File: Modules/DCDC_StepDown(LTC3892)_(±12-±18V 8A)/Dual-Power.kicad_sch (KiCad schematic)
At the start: 81 parts, among them J1 Conn_02x05_Top_Bottom, J2 Conn_02x05_Top_Bottom, J3 Conn_01x02, Q1 BSC028N06LS3, Q2 BSC028N06LS3, Q3 BSC028N06LS3, Q4 BSC028N06LS3, Q5 BSC028N06LS3, U1 LTC3892EUHPBF, U2 LT1797

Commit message: update Dual-Power components value
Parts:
- C4: value 2.2uF -> 4.7uF
- Cl1, Cl2: value OPT -> 100uF
- Cx1, Cx4, Cx5: value OPT -> 4.7uF
- Cx2, Cx3: value OPT -> 2.2uF
- Cx6, Cx7: value OPT -> 10uF
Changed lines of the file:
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@@
       (effects (font (size 1.27 1.27)) (justify left))
     )
-    (property "Value" "2.2uF" (id 1) (at 163.83 96.52 0)
+    (property "Value" "4.7uF" (id 1) (at 163.83 96.52 0)
       (effects (font (size 1.27 1.27)) (justify left))
     )
@@
       (effects (font (size 1.27 1.27)) (justify left))
     )
-    (property "Value" "OPT" (id 1) (at 330.2 52.07 0)
+    (property "Value" "4.7uF" (id 1) (at 330.2 52.07 0)
       (effects (font (size 1.27 1.27)) (justify left))
     )
@@
       (effects (font (size 1.27 1.27)) (justify left))
     )
-    (property "Value" "OPT" (id 1) (at 336.55 52.07 0)
+    (property "Value" "2.2uF" (id 1) (at 336.55 52.07 0)
       (effects (font (size 1.27 1.27)) (justify left))
     )
@@
       (effects (font (size 1.27 1.27)) (justify left))
     )
-    (property "Value" "OPT" (id 1) (at 342.9 52.07 0)
+    (property "Value" "2.2uF" (id 1) (at 342.9 52.07 0)
       (effects (font (size 1.27 1.27)) (justify left))
     )
@@
       (effects (font (size 1.27 1.27)) (justify left))
     )
-    (property "Value" "OPT" (id 1) (at 349.25 52.07 0)
+    (property "Value" "4.7uF" (id 1) (at 349.25 52.07 0)
       (effects (font (size 1.27 1.27)) (justify left))
     )
@@
       (effects (font (size 1.27 1.27)) (justify left))
     )
-    (property "Value" "OPT" (id 1) (at 355.6 52.07 0)
+    (property "Value" "4.7uF" (id 1) (at 355.6 52.07 0)
       (effects (font (size 1.27 1.27)) (justify left))
     )
@@
       (effects (font (size 1.27 1.27)) (justify left))
     )
-    (property "Value" "OPT" (id 1) (at 361.95 52.07 0)
+    (property "Value" "10uF" (id 1) (at 361.95 52.07 0)
       (effects (font (size 1.27 1.27)) (justify left))
     )
@@
       (effects (font (size 1.27 1.27)) (justify left))
     )
-    (property "Value" "OPT" (id 1) (at 368.3 52.07 0)
+    (property "Value" "10uF" (id 1) (at 368.3 52.07 0)
       (effects (font (size 1.27 1.27)) (justify left))
     )
@@
       (effects (font (size 1.27 1.27)) (justify right))
     )
-    (property "Value" "150uF" (id 1) (at 337.82 191.77 0)
+    (property "Value" "150uF" (id 1) (at 332.74 191.77 0)
       (effects (font (size 1.27 1.27)) (justify right))
     )
@@
       (effects (font (size 1.27 1.27)) (justify left))
     )
-    (property "Value" "OPT" (id 1) (at 372.11 52.07 0)
+    (property "Value" "100uF" (id 1) (at 372.11 52.07 0)
       (effects (font (size 1.27 1.27)) (justify left))
     )
@@
       (effects (font (size 1.27 1.27)) (justify left))
     )
-    (property "Value" "OPT" (id 1) (at 378.46 52.07 0)
+    (property "Value" "100uF" (id 1) (at 378.46 52.07 0)
       (effects (font (size 1.27 1.27)) (justify left))
     )
@@
     )
     (path "/00000000-0000-0000-0000-0000616375a2"
-      (reference "C4") (unit 1) (value "2.2uF") (footprint "Capacitor_SMD:C_1206_3216Metric")
+      (reference "C4") (unit 1) (value "4.7uF") (footprint "Capacitor_SMD:C_1206_3216Metric")
     )
     (path "/00000000-0000-0000-0000-0000616da52e"
@@
     )
     (path "/00000000-0000-0000-0000-0000617a732d"
-      (reference "Cl1") (unit 1) (value "OPT") (footprint "Capacitor_SMD:CP_Elec_10x10")
+      (reference "Cl1") (unit 1) (value "100uF") (footprint "Capacitor_SMD:CP_Elec_10x10")
     )
     (path "/00000000-0000-0000-0000-0000617a7327"
-      (reference "Cl2") (unit 1) (value "OPT") (footprint "Capacitor_SMD:CP_Elec_10x10")
+      (reference "Cl2") (unit 1) (value "100uF") (footprint "Capacitor_SMD:CP_Elec_10x10")
     )
     (path "/00000000-0000-0000-0000-0000617046a1"
-      (reference "Cx1") (unit 1) (value "OPT") (footprint "Capacitor_SMD:C_1206_3216Metric")
+      (reference "Cx1") (unit 1) (value "4.7uF") (footprint "Capacitor_SMD:C_1206_3216Metric")
     )
     (path "/00000000-0000-0000-0000-00006170469b"
-      (reference "Cx2") (unit 1) (value "OPT") (footprint "Capacitor_SMD:C_1206_3216Metric")
+      (reference "Cx2") (unit 1) (value "2.2uF") (footprint "Capacitor_SMD:C_1206_3216Metric")
     )
     (path "/00000000-0000-0000-0000-0000617dce4e"
-      (reference "Cx3") (unit 1) (value "OPT") (footprint "Capacitor_SMD:C_1206_3216Metric")
+      (reference "Cx3") (unit 1) (value "2.2uF") (footprint "Capacitor_SMD:C_1206_3216Metric")
     )
     (path "/00000000-0000-0000-0000-0000617dce48"
-      (reference "Cx4") (unit 1) (value "OPT") (footprint "Capacitor_SMD:C_1206_3216Metric")
+      (reference "Cx4") (unit 1) (value "4.7uF") (footprint "Capacitor_SMD:C_1206_3216Metric")
     )
     (path "/00000000-0000-0000-0000-0000618152fa"
-      (reference "Cx5") (unit 1) (value "OPT") (footprint "Capacitor_SMD:C_1206_3216Metric")
+      (reference "Cx5") (unit 1) (value "4.7uF") (footprint "Capacitor_SMD:C_1206_3216Metric")
     )
     (path "/00000000-0000-0000-0000-0000618152f4"
-      (reference "Cx6") (unit 1) (value "OPT") (footprint "Capacitor_SMD:C_1206_3216Metric")
+      (reference "Cx6") (unit 1) (value "10uF") (footprint "Capacitor_SMD:C_1206_3216Metric")
     )
     (path "/00000000-0000-0000-0000-000061871b5c"
-      (reference "Cx7") (unit 1) (value "OPT") (footprint "Capacitor_SMD:C_1206_3216Metric")
+      (reference "Cx7") (unit 1) (value "10uF") (footprint "Capacitor_SMD:C_1206_3216Metric")
     )
     (path "/00000000-0000-0000-0000-00006158ce04"

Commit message: fix description in Dual-Power.kicad_sch
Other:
- note added: "Q1\Q2\Q5 BSC028N OR BSC026N(Rec) Q3\Q4\ BSC100N OR BSC117N(Rec)"
- note removed: "Q1\Q2\Q5 BSC028N OR BSC026N Q3\Q4 BSC100N OR BSC117N"
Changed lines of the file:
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@@
+    (stroke (width 0) (type default) (color 0 0 0 0))
+  )
+  (polyline (pts (xy 264.16 199.39) (xy 303.53 199.39))
+    (stroke (width 0) (type default) (color 0 0 0 0))
+  )
+  (polyline (pts (xy 264.16 213.36) (xy 264.16 199.39))
     (stroke (width 0) (type default) (color 0 0 0 0))
   )
@@
     (stroke (width 0) (type default) (color 0 0 0 0))
   )
-  (polyline (pts (xy 265.43 196.85) (xy 300.99 196.85))
-    (stroke (width 0) (type default) (color 0 0 0 0))
-  )
-  (polyline (pts (xy 265.43 210.82) (xy 265.43 196.85))
-    (stroke (width 0) (type default) (color 0 0 0 0))
-  )
   (polyline (pts (xy 275.59 177.8) (xy 275.59 181.61))
     (stroke (width 0) (type default) (color 0 0 0 0))
@@
     (stroke (width 0) (type default) (color 0 0 0 0))
   )
-  (polyline (pts (xy 300.99 196.85) (xy 300.99 210.82))
+  (polyline (pts (xy 303.53 199.39) (xy 303.53 213.36))
     (stroke (width 0) (type default) (color 0 0 0 0))
   )
-  (polyline (pts (xy 300.99 210.82) (xy 265.43 210.82))
+  (polyline (pts (xy 303.53 213.36) (xy 264.16 213.36))
     (stroke (width 0) (type default) (color 0 0 0 0))
   )
@@
     (effects (font (size 1.27 1.27) (thickness 0.254) bold) (justify left bottom))
   )
-  (text "Group1: Q3 Q2 R14\nGroup2: Q4 Q5 R17 (Optional)" (at 266.7 201.93 0)
+  (text "Group1: Q3 Q2 R14\nGroup2: Q4 Q5 R17 (Optional)" (at 265.43 204.47 0)
     (effects (font (size 1.27 1.27)) (justify left bottom))
   )
-  (text "Q1\\Q2\\Q5 BSC028N OR BSC026N\nQ3\\Q4 BSC100N OR BSC117N"
-    (at 266.7 208.28 0)
+  (text "Q1\\Q2\\Q5 BSC028N OR BSC026N(Rec)\nQ3\\Q4\\   BSC100N OR BSC117N(Rec)"
+    (at 265.43 210.82 0)
     (effects (font (size 1.27 1.27)) (justify left bottom))
   )

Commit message: continue..
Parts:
- Q1, Q2, Q5: value BSC028N06LS3 -> BSC026N08NS5; symbol Transistor_FET:BSC028N06LS3 -> Transistor_FET:BSC026N08NS5
- Q3, Q4: value BSC028N06LS3 -> BSC117N08NS5; symbol Transistor_FET:BSC028N06LS3 -> Transistor_FET:BSC117N08NS5
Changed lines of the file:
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@@
     (pin "4")
   )
-  (symbol (lib_id "Transistor_FET:BSC028N06LS3") (at 168.91 179.07 180) (unit 1)
+  (symbol (lib_id "Transistor_FET:BSC026N08NS5") (at 168.91 179.07 180) (unit 1)
     (in_bom yes) (on_board yes)
     (property "Reference" "Q1" (id 0) (at 163.703 179.07 0)
       (effects (font (size 1.27 1.27)) (justify left))
     )
-    (property "Value" "BSC028N06LS3" (id 1) (at 163.7284 177.927 0)
+    (property "Value" "BSC026N08NS5" (id 1) (at 163.7284 177.927 0)
       (effects (font (size 1.27 1.27)) (justify left) hide)
     )
@@
       (effects (font (size 1.27 1.27) italic) (justify left) hide)
     )
-    (property "Datasheet" "http://www.infineon.com/dgdl/Infineon-BSC028N06LS3-DS-v02_02-en.pdf?fileId=db3a30431ddc9372011ebafa4c607f8c" (id 3) (at 168.91 179.07 90)
-      (effects (font (size 1.27 1.27)) (justify left) hide)
-    )
-    (pin "1")
-    (pin "2")
-    (pin "3")
-    (pin "4")
-    (pin "5")
-  )
-  (symbol (lib_id "Transistor_FET:BSC028N06LS3") (at 245.11 179.07 0) (unit 1)
+    (property "Datasheet" "http://www.infineon.com/dgdl/Infineon-BSC026N08NS5-DS-v02_01-EN.pdf?fileId=5546d4624ad04ef9014ae2eace7629e0" (id 3) (at 168.91 179.07 90)
+      (effects (font (size 1.27 1.27)) (justify left) hide)
+    )
+    (pin "1")
+    (pin "2")
+    (pin "3")
+    (pin "4")
+    (pin "5")
+  )
+  (symbol (lib_id "Transistor_FET:BSC117N08NS5") (at 245.11 179.07 0) (unit 1)
     (in_bom yes) (on_board yes)
     (property "Reference" "Q3" (id 0) (at 242.57 182.88 0)
       (effects (font (size 1.27 1.27)) (justify left))
     )
-    (property "Value" "BSC028N06LS3" (id 1) (at 250.2916 180.213 0)
+    (property "Value" "BSC117N08NS5" (id 1) (at 250.2916 180.213 0)
       (effects (font (size 1.27 1.27)) (justify left) hide)
     )
@@
       (effects (font (size 1.27 1.27) italic) (justify left) hide)
     )
-    (property "Datasheet" "http://www.infineon.com/dgdl/Infineon-BSC028N06LS3-DS-v02_02-en.pdf?fileId=db3a30431ddc9372011ebafa4c607f8c" (id 3) (at 245.11 179.07 90)
-      (effects (font (size 1.27 1.27)) (justify left) hide)
-    )
-    (pin "1")
-    (pin "2")
-    (pin "3")
-    (pin "4")
-    (pin "5")
-  )
-  (symbol (lib_id "Transistor_FET:BSC028N06LS3") (at 245.11 203.2 0) (unit 1)
+    (property "Datasheet" "http://www.infineon.com/dgdl/Infineon-BSC117N08NS5-DS-v02_00-EN.pdf?fileId=5546d4624ad04ef9014ae97632721c1b" (id 3) (at 245.11 179.07 90)
+      (effects (font (size 1.27 1.27)) (justify left) hide)
+    )
+    (pin "1")
+    (pin "2")
+    (pin "3")
+    (pin "4")
+    (pin "5")
+  )
+  (symbol (lib_id "Transistor_FET:BSC026N08NS5") (at 245.11 203.2 0) (unit 1)
     (in_bom yes) (on_board yes)
     (property "Reference" "Q2" (id 0) (at 242.57 199.39 0)
       (effects (font (size 1.27 1.27)) (justify left))
     )
-    (property "Value" "BSC028N06LS3" (id 1) (at 250.2916 204.343 0)
+    (property "Value" "BSC026N08NS5" (id 1) (at 250.2916 204.343 0)
       (effects (font (size 1.27 1.27)) (justify left) hide)
     )
@@
       (effects (font (size 1.27 1.27) italic) (justify left) hide)
     )
-    (property "Datasheet" "http://www.infineon.com/dgdl/Infineon-BSC028N06LS3-DS-v02_02-en.pdf?fileId=db3a30431ddc9372011ebafa4c607f8c" (id 3) (at 245.11 203.2 90)
-      (effects (font (size 1.27 1.27)) (justify left) hide)
-    )
-    (pin "1")
-    (pin "2")
-    (pin "3")
-    (pin "4")
-    (pin "5")
-  )
-  (symbol (lib_id "Transistor_FET:BSC028N06LS3") (at 257.81 179.07 0) (unit 1)
+    (property "Datasheet" "http://www.infineon.com/dgdl/Infineon-BSC026N08NS5-DS-v02_01-EN.pdf?fileId=5546d4624ad04ef9014ae2eace7629e0" (id 3) (at 245.11 203.2 90)
+      (effects (font (size 1.27 1.27)) (justify left) hide)
+    )
+    (pin "1")
+    (pin "2")
+    (pin "3")
+    (pin "4")
+    (pin "5")
+  )
+  (symbol (lib_id "Transistor_FET:BSC117N08NS5") (at 257.81 179.07 0) (unit 1)
     (in_bom yes) (on_board yes)
     (property "Reference" "Q4" (id 0) (at 255.27 182.88 0)
       (effects (font (size 1.27 1.27)) (justify left))
     )
-    (property "Value" "BSC028N06LS3" (id 1) (at 262.9916 180.213 0)
+    (property "Value" "BSC117N08NS5" (id 1) (at 262.9916 180.213 0)
       (effects (font (size 1.27 1.27)) (justify left) hide)
     )
@@
       (effects (font (size 1.27 1.27) italic) (justify left) hide)
     )
-    (property "Datasheet" "http://www.infineon.com/dgdl/Infineon-BSC028N06LS3-DS-v02_02-en.pdf?fileId=db3a30431ddc9372011ebafa4c607f8c" (id 3) (at 257.81 179.07 90)
-      (effects (font (size 1.27 1.27)) (justify left) hide)
-    )
-    (pin "1")
-    (pin "2")
-    (pin "3")
-    (pin "4")
-    (pin "5")
-  )
-  (symbol (lib_id "Transistor_FET:BSC028N06LS3") (at 257.81 203.2 0) (unit 1)
+    (property "Datasheet" "http://www.infineon.com/dgdl/Infineon-BSC117N08NS5-DS-v02_00-EN.pdf?fileId=5546d4624ad04ef9014ae97632721c1b" (id 3) (at 257.81 179.07 90)
+      (effects (font (size 1.27 1.27)) (justify left) hide)
+    )
+    (pin "1")
+    (pin "2")
+    (pin "3")
+    (pin "4")
+    (pin "5")
+  )
+  (symbol (lib_id "Transistor_FET:BSC026N08NS5") (at 257.81 203.2 0) (unit 1)
     (in_bom yes) (on_board yes)
     (property "Reference" "Q5" (id 0) (at 255.27 199.39 0)
       (effects (font (size 1.27 1.27)) (justify left))
     )
-    (property "Value" "BSC028N06LS3" (id 1) (at 262.9916 204.343 0)
+    (property "Value" "BSC026N08NS5" (id 1) (at 262.9916 204.343 0)
       (effects (font (size 1.27 1.27)) (justify left) hide)
     )
@@
       (effects (font (size 1.27 1.27) italic) (justify left) hide)
     )
-    (property "Datasheet" "http://www.infineon.com/dgdl/Infineon-BSC028N06LS3-DS-v02_02-en.pdf?fileId=db3a30431ddc9372011ebafa4c607f8c" (id 3) (at 257.81 203.2 90)
+    (property "Datasheet" "http://www.infineon.com/dgdl/Infineon-BSC026N08NS5-DS-v02_01-EN.pdf?fileId=5546d4624ad04ef9014ae2eace7629e0" (id 3) (at 257.81 203.2 90)
       (effects (font (size 1.27 1.27)) (justify left) hide)
     )
@@
     )
     (path "/00000000-0000-0000-0000-00006185bead"
-      (reference "Q1") (unit 1) (value "BSC028N06LS3") (footprint "Package_TO_SOT_SMD:TDSON-8-1")
+      (reference "Q1") (unit 1) (value "BSC026N08NS5") (footprint "Package_TO_SOT_SMD:TDSON-8-1")
     )
     (path "/00000000-0000-0000-0000-00006156edf6"
-      (reference "Q2") (unit 1) (value "BSC028N06LS3") (footprint "Package_TO_SOT_SMD:TDSON-8-1")
+      (reference "Q2") (unit 1) (value "BSC026N08NS5") (footprint "Package_TO_SOT_SMD:TDSON-8-1")
     )
     (path "/00000000-0000-0000-0000-00006167a267"
-      (reference "Q3") (unit 1) (value "BSC028N06LS3") (footprint "Package_TO_SOT_SMD:TDSON-8-1")
+      (reference "Q3") (unit 1) (value "BSC117N08NS5") (footprint "Package_TO_SOT_SMD:TDSON-8-1")
     )
     (path "/00000000-0000-0000-0000-00006160bac2"
-      (reference "Q4") (unit 1) (value "BSC028N06LS3") (footprint "Package_TO_SOT_SMD:TDSON-8-1")
+      (reference "Q4") (unit 1) (value "BSC117N08NS5") (footprint "Package_TO_SOT_SMD:TDSON-8-1")
     )
     (path "/00000000-0000-0000-0000-00006162e77f"
-      (reference "Q5") (unit 1) (value "BSC028N06LS3") (footprint "Package_TO_SOT_SMD:TDSON-8-1")
+      (reference "Q5") (unit 1) (value "BSC026N08NS5") (footprint "Package_TO_SOT_SMD:TDSON-8-1")
     )
     (path "/00000000-0000-0000-0000-0000615fa318"

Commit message: DCDC_StepDown(TLC3892) > fix capacity value
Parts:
- C4: value 4.7uF -> 2.2uF
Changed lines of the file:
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@@
       (effects (font (size 1.27 1.27)) (justify left))
     )
-    (property "Value" "4.7uF" (id 1) (at 163.83 96.52 0)
+    (property "Value" "2.2uF" (id 1) (at 163.83 96.52 0)
       (effects (font (size 1.27 1.27)) (justify left))
     )
@@
     )
     (path "/00000000-0000-0000-0000-0000616375a2"
-      (reference "C4") (unit 1) (value "4.7uF") (footprint "Capacitor_SMD:C_1206_3216Metric")
+      (reference "C4") (unit 1) (value "2.2uF") (footprint "Capacitor_SMD:C_1206_3216Metric")
     )
     (path "/00000000-0000-0000-0000-0000616da52e"

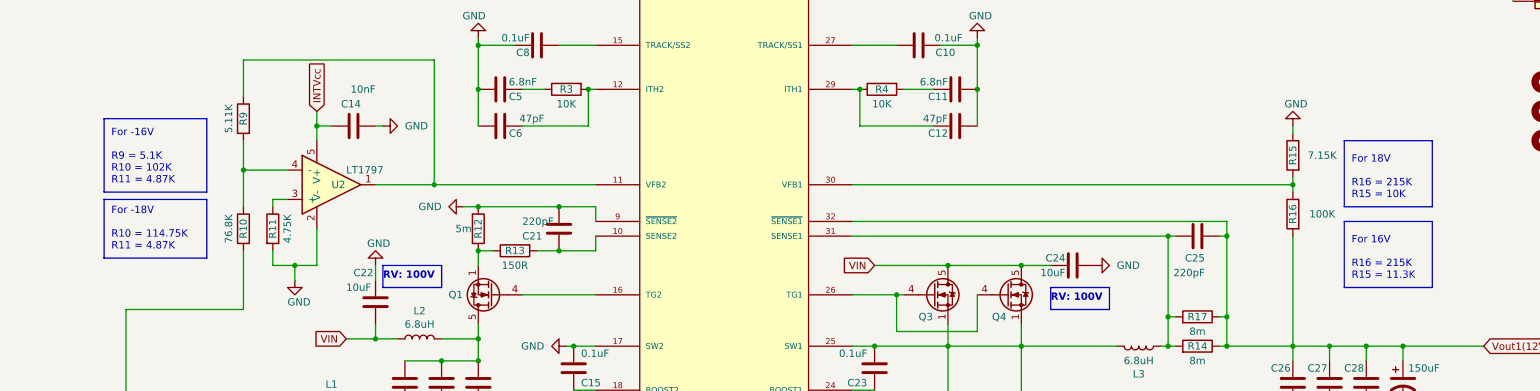
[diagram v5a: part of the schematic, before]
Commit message: Update description in Sch
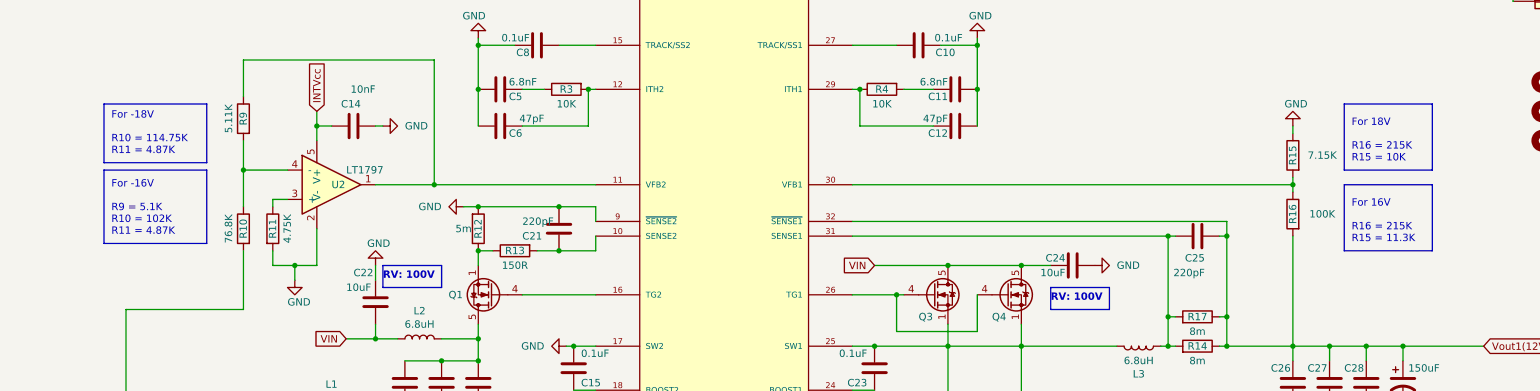
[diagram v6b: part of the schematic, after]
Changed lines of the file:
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@@
     (stroke (width 0) (type default) (color 0 0 0 0))
   )
-  (polyline (pts (xy 316.23 177.8) (xy 331.47 177.8))
+  (polyline (pts (xy 316.23 171.45) (xy 331.47 171.45))
     (stroke (width 0) (type default) (color 0 0 0 0))
   )
@@
     (stroke (width 0) (type default) (color 0 0 0 0))
   )
-  (polyline (pts (xy 316.23 166.37) (xy 316.23 177.8))
+  (polyline (pts (xy 316.23 160.02) (xy 316.23 171.45))
     (stroke (width 0) (type default) (color 0 0 0 0))
   )
@@
     (stroke (width 0) (type default) (color 0 0 0 0))
   )
-  (polyline (pts (xy 331.47 163.83) (xy 331.47 152.4))
+  (polyline (pts (xy 331.47 157.48) (xy 331.47 146.05))
     (stroke (width 0) (type default) (color 0 0 0 0))
   )
@@
     (stroke (width 0) (type default) (color 0 0 0 0))
   )
-  (polyline (pts (xy 101.6 172.72) (xy 119.38 172.72))
+  (polyline (pts (xy 101.6 156.21) (xy 119.38 156.21))
     (stroke (width 0) (type default) (color 0 0 0 0))
   )
@@
     (stroke (width 0) (type default) (color 0 0 0 0))
   )
-  (polyline (pts (xy 119.38 148.59) (xy 101.6 148.59))
+  (polyline (pts (xy 119.38 157.48) (xy 101.6 157.48))
     (stroke (width 0) (type default) (color 0 0 0 0))
   )
@@
     (stroke (width 0) (type default) (color 0 0 0 0))
   )
-  (polyline (pts (xy 101.6 148.59) (xy 101.6 161.29))
+  (polyline (pts (xy 101.6 157.48) (xy 101.6 170.18))
     (stroke (width 0) (type default) (color 0 0 0 0))
   )
@@
     (stroke (width 0) (type default) (color 0 0 0 0))
   )
-  (polyline (pts (xy 119.38 162.56) (xy 101.6 162.56))
+  (polyline (pts (xy 119.38 146.05) (xy 101.6 146.05))
     (stroke (width 0) (type default) (color 0 0 0 0))
   )
@@
     (stroke (width 0) (type default) (color 0 0 0 0))
   )
-  (polyline (pts (xy 101.6 161.29) (xy 119.38 161.29))
+  (polyline (pts (xy 101.6 170.18) (xy 119.38 170.18))
     (stroke (width 0) (type default) (color 0 0 0 0))
   )
@@
     (stroke (width 0) (type default) (color 0 0 0 0))
   )
-  (polyline (pts (xy 101.6 162.56) (xy 101.6 172.72))
+  (polyline (pts (xy 101.6 146.05) (xy 101.6 156.21))
     (stroke (width 0) (type default) (color 0 0 0 0))
   )
@@
     (stroke (width 0) (type default) (color 0 0 0 0))
   )
-  (polyline (pts (xy 331.47 177.8) (xy 331.47 166.37))
+  (polyline (pts (xy 331.47 171.45) (xy 331.47 160.02))
     (stroke (width 0) (type default) (color 0 0 0 0))
   )
@@
     (stroke (width 0) (type default) (color 0 0 0 0))
   )
-  (polyline (pts (xy 119.38 172.72) (xy 119.38 162.56))
+  (polyline (pts (xy 119.38 156.21) (xy 119.38 146.05))
     (stroke (width 0) (type default) (color 0 0 0 0))
   )
@@
     (stroke (width 0) (type default) (color 0 0 0 0))
   )
-  (polyline (pts (xy 316.23 152.4) (xy 316.23 163.83))
+  (polyline (pts (xy 316.23 146.05) (xy 316.23 157.48))
     (stroke (width 0) (type default) (color 0 0 0 0))
   )
@@
     (stroke (width 0) (type default) (color 0 0 0 0))
   )
-  (polyline (pts (xy 331.47 166.37) (xy 316.23 166.37))
+  (polyline (pts (xy 331.47 160.02) (xy 316.23 160.02))
     (stroke (width 0) (type default) (color 0 0 0 0))
   )
@@
     (stroke (width 0) (type default) (color 0 0 0 0))
   )
-  (polyline (pts (xy 119.38 161.29) (xy 119.38 148.59))
+  (polyline (pts (xy 119.38 170.18) (xy 119.38 157.48))
     (stroke (width 0) (type default) (color 0 0 0 0))
   )
@@
     (stroke (width 0) (type default) (color 0 0 0 0))
   )
-  (polyline (pts (xy 316.23 163.83) (xy 331.47 163.83))
+  (polyline (pts (xy 316.23 157.48) (xy 331.47 157.48))
     (stroke (width 0) (type default) (color 0 0 0 0))
   )
@@
     (stroke (width 0) (type default) (color 0 0 0 0))
   )
-  (polyline (pts (xy 331.47 152.4) (xy 316.23 152.4))
+  (polyline (pts (xy 331.47 146.05) (xy 316.23 146.05))
     (stroke (width 0) (type default) (color 0 0 0 0))
   )
@@
     (stroke (width 0) (type default) (color 0 0 0 0))
   )
-  (text "For 18V\n\nR16 = 215K\nR15 = 10K" (at 317.5 162.56 0)
+  (text "For 18V\n\nR16 = 215K\nR15 = 10K" (at 317.5 156.21 0)
     (effects (font (size 1.27 1.27)) (justify left bottom))
   )
-  (text "For -18V\n\nR10 = 114.75K\nR11 = 4.87K" (at 102.87 171.45 0)
+  (text "For -18V\n\nR10 = 114.75K\nR11 = 4.87K" (at 102.87 154.94 0)
     (effects (font (size 1.27 1.27)) (justify left bottom))
   )
@@
     (effects (font (size 1.27 1.27) (thickness 0.254) bold) (justify left bottom))
   )
-  (text "For -16V\n\nR9 = 5.1K\nR10 = 102K\nR11 = 4.87K" (at 102.87 160.02 0)
+  (text "For -16V\n\nR9 = 5.1K\nR10 = 102K\nR11 = 4.87K" (at 102.87 168.91 0)
     (effects (font (size 1.27 1.27)) (justify left bottom))
   )
@@
     (effects (font (size 1.27 1.27)) (justify left bottom))
   )
-  (text "For 16V\n\nR16 = 215K\nR15 = 11.3K" (at 317.5 176.53 0)
+  (text "For 16V\n\nR16 = 215K\nR15 = 11.3K" (at 317.5 170.18 0)
     (effects (font (size 1.27 1.27)) (justify left bottom))
   )
